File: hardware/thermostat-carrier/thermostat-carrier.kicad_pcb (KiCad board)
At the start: 2 copper layers, 100 x 100 mm, 82 parts, among them J1 24 VAC, J2 Calls 24 VAC, J3 USB-C 5 V in, J4 USB-A 5 V to display, J5 Display I2C, J6 Display IO6, J7 Room SHT45 (Qwiic), K1 AQV252G, K2 AQV252G, K3 AQV252G, K4 AQV252G, K5 AQV252G, K6 AQV252G, U1 LM2596HV, U10 H11AA1, U11 H11AA1, U12 H11AA1, U2 AMS1117-3.3, U3 MCP23017-E/SO, U4 TPS3823-33, U5 SC18IS602B, U6 Wio-SX1262, U7 H11AA1, U8 H11AA1, U9 H11AA1

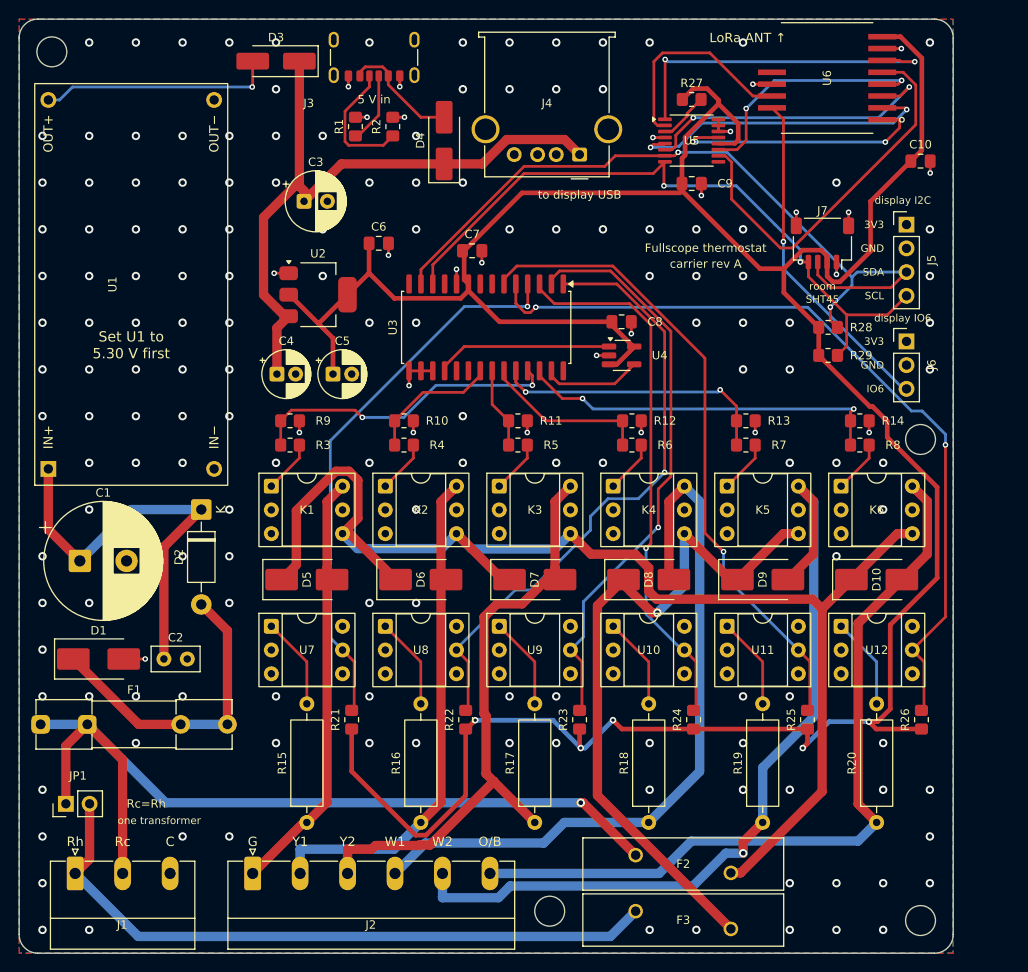
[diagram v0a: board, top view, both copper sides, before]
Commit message: Thermostat carrier: stack behind the Waveshare 4.3 on its own outline
The carrier now matches the display's 106 x 68 mm outline and screws to its
four M2.5 standoffs (measured from Waveshare's STEP model). SMD parts sit on
the wall side for JLC assembly; a right-edge notch clears the display's side
sockets, and short HY2.0 leads go to J5 (I2C) and J6 (IO6 for LoRa DIO1).

- Power: TPS54360B buck to 5.3 V replaces the LM2596 module; USB-C in for
  display-only use, USB-C out carries 5 V to the display.
- route.py: fan-out vias stay inside the outline and off exposed pads;
  pour islands are joined by vias, short bridges or a grid search
  (maze_bridge) for a GND track.
- gen_sch: PWR_FLAG on label nets (flag_nets) for the buck's VRAW input.
- make_fab: all-SMD JLC CPL/BOM for the thermostat carrier.
- DRC 0 violations, 0 unconnected, schematic parity clean; ERC clean.

Co-Authored-By: Claude Opus 5.5 <noreply@anthropic.com>
Claude-Session: https://claude.ai/code/session_011hFUPCDAe7urxnoDwvZQtt
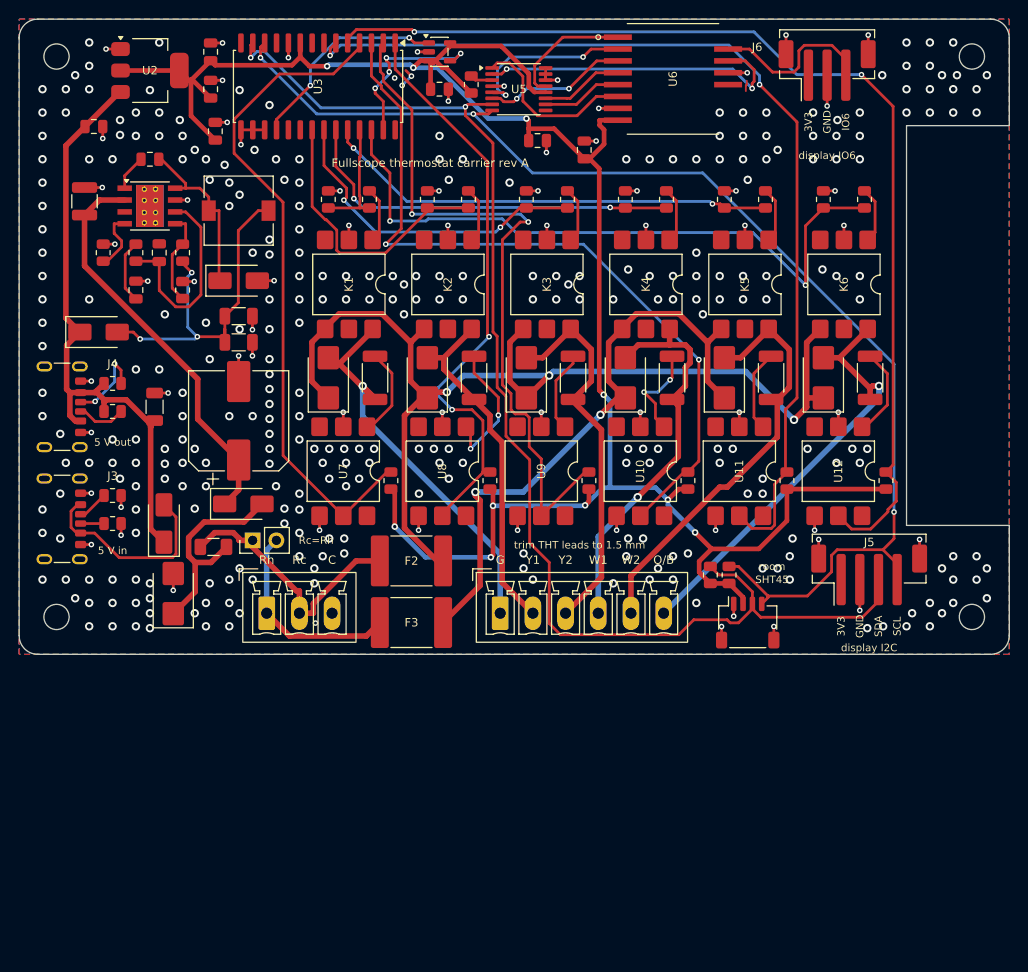
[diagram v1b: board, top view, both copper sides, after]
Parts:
- added C11: 0.1µF, Capacitor_SMD:C_0805_2012Metric, F.Cu at (64.0, 65.0)
- added C12: 22nF, Capacitor_SMD:C_0805_2012Metric, F.Cu at (62.5, 79.0)
- added C13: 100pF, Capacitor_SMD:C_0805_2012Metric, F.Cu at (65.0, 75.0)
- added C14: 22µF 16V, Capacitor_SMD:C_1206_3216Metric, F.Cu at (73.5, 81.8)
- added C15: 22µF 16V, Capacitor_SMD:C_1206_3216Metric, F.Cu at (73.5, 84.6)
- added D11: SS36, Diode_SMD:D_SMA, F.Cu at (73.5, 78.0)
- added L1: 22µH 2A, Inductor_SMD:L_7.3x7.3_H4.5, F.Cu at (73.5, 70.5)
- added R30: 243k, Resistor_SMD:R_0805_2012Metric, F.Cu at (59.0, 75.0)
- added R31: 56k, Resistor_SMD:R_0805_2012Metric, F.Cu at (67.5, 75.0)
- added R32: 10k, Resistor_SMD:R_0805_2012Metric, F.Cu at (67.5, 79.0)
- added R33: 6.8k, Resistor_SMD:R_0805_2012Metric, F.Cu at (62.5, 75.0)
- added R34: 56k, Resistor_SMD:R_0805_2012Metric, F.Cu at (60.0, 89.0)
- added R35: 56k, Resistor_SMD:R_0805_2012Metric, F.Cu at (60.0, 92.0)
- C1: value 1000µF 63V -> 220µF 63V; footprint Capacitor_THT:CP_Radial_D12.5mm_P5.00mm -> Capacitor_SMD:CP_Elec_10x10.5
- C10, C6, C7, C8, C9: footprint Capacitor_SMD:C_0805_2012Metric_Pad1.18x1.45mm_HandSolder -> Capacitor_SMD:C_0805_2012Metric
- C2: value 0.1µF -> 2.2µF 100V; footprint Capacitor_THT:C_Disc_D5.0mm_W2.5mm_P2.50mm -> Capacitor_SMD:C_1210_3225Metric
- C3: value 220µF 16V -> 22µF 16V; footprint Capacitor_THT:CP_Radial_D6.3mm_P2.50mm -> Capacitor_SMD:C_1206_3216Metric
- C4: value 10µF 16V -> 10µF 25V; footprint Capacitor_THT:CP_Radial_D5.0mm_P2.00mm -> Capacitor_SMD:C_0805_2012Metric
- C5: footprint Capacitor_THT:CP_Radial_D5.0mm_P2.00mm -> Capacitor_SMD:C_0805_2012Metric
- D1: value SMBJ48CA -> SMBJ40CA; footprint Diode_SMD:D_SMB_Handsoldering -> Diode_SMD:D_SMB
- D10, D5, D6, D7, D8, D9: footprint Diode_SMD:D_SMB_Handsoldering -> Diode_SMD:D_SMB
- D2: value 1N4007 -> S1M; footprint Diode_THT:D_DO-41_SOD81_P10.16mm_Horizontal -> Diode_SMD:D_SMA
- D3, D4: footprint Diode_SMD:D_SMA_Handsoldering -> Diode_SMD:D_SMA
- F1: value 0.5 A fast -> 0.5 A fast 63 V; footprint Fuse:Fuseholder_Clip-5x20mm_Littelfuse_111_Inline_P20.00x5.00mm_D1.05mm_Horizontal -> Fuse:Fuse_1206_3216Metric
- F2, F3: value 0ZRE0125FF -> 2920L110/60; footprint Fuse:Fuse_BelFuse_0ZRE0125FF_L21.2mm_W5.3mm -> Fuse:Fuse_2920_7451Metric
- H1, H2, H3, H4: value M3 -> M2.5; footprint MountingHole:MountingHole_3.2mm_M3_DIN965 -> MountingHole:MountingHole_2.7mm_M2.5_DIN965
- J1: footprint Connector_Phoenix_MC_HighVoltage:PhoenixContact_MC_1,5_3-G-5.08_1x03_P5.08mm_Horizontal -> Connector_Phoenix_MC:PhoenixContact_MCV_1,5_3-G-3.5_1x03_P3.50mm_Vertical
- J2: footprint Connector_Phoenix_MC_HighVoltage:PhoenixContact_MC_1,5_6-G-5.08_1x06_P5.08mm_Horizontal -> Connector_Phoenix_MC:PhoenixContact_MCV_1,5_6-G-3.5_1x06_P3.50mm_Vertical
- J4: value USB-A 5 V to display -> USB-C 5 V to display; footprint Connector_USB:USB_A_Molex_67643_Horizontal -> Connector_USB:USB_C_Receptacle_GCT_USB4125-xx-x_6P_TopMnt_Horizontal
- J5: footprint Connector_PinHeader_2.54mm:PinHeader_1x04_P2.54mm_Vertical -> Connector_JST:JST_PH_B4B-PH-SM4-TB_1x04-1MP_P2.00mm_Vertical
- J6: footprint Connector_PinHeader_2.54mm:PinHeader_1x03_P2.54mm_Vertical -> Connector_JST:JST_PH_B3B-PH-SM4-TB_1x03-1MP_P2.00mm_Vertical
- K1, K2, K3, K4, K5, K6: value AQV252G -> AQV252GS; footprint Package_DIP:DIP-6_W7.62mm_Socket -> Package_DIP:SMDIP-6_W9.53mm
- R1, R10, R11, R12, R13, R14, R2, R21, R22, R23, R24, R25, R26, R27, R28, R29, R3, R4, R5, R6, R7, R8, R9: footprint Resistor_SMD:R_0805_2012Metric_Pad1.20x1.40mm_HandSolder -> Resistor_SMD:R_0805_2012Metric
- R15, R16, R17, R18, R19, R20: value 4.7k ½W -> 4.7k 2010; footprint Resistor_THT:R_Axial_DIN0309_L9.0mm_D3.2mm_P12.70mm_Horizontal -> Resistor_SMD:R_2010_5025Metric
- U1: value LM2596HV -> TPS54360BDDAR; footprint hvac_carrier:LM2596HVS_Module -> Package_SO:TI_SO-PowerPAD-8_ThermalVias
- U10, U11, U12, U7, U8, U9: value H11AA1 -> H11AA1SM; footprint Package_DIP:DIP-6_W7.62mm_Socket -> Package_DIP:SMDIP-6_W9.53mm
- U4: footprint Package_TO_SOT_SMD:SOT-23-5_HandSoldering -> Package_TO_SOT_SMD:SOT-23-5
- moved H3 94.4 mm to (54.0, 114.0)
- moved H2 92.7 mm to (152.0, 54.0)
- moved J4 62.6 mm to (53.5, 91.5), turned to -90 degrees
- moved J3 61.2 mm to (53.5, 103.5), turned to -90 degrees
- moved H4 55.1 mm to (152.0, 114.0)
- moved R2 52.0 mm to (60.0, 104.0), turned to 0 degrees
- moved D4 50.8 mm to (65.5, 104.0)
- moved C2 49.7 mm to (57.0, 69.5), turned to 90 degrees
- moved R15 48.2 mm to (88.1, 88.4)
- moved R16 47.9 mm to (98.7, 88.4)
- moved R17 47.8 mm to (109.3, 88.4)
- moved R18 47.7 mm to (119.9, 88.4)
- moved R19 47.6 mm to (130.5, 88.4)
- moved R20 47.6 mm to (141.1, 88.4)
- moved R1 47.3 mm to (60.0, 101.0), turned to 0 degrees
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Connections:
- U1 pad 1: /VRAW -> /BOOT
- U1 pad 2: GND -> /VRAW
- U1 pad 3: /V5_BUCK -> unconnected-(U1-EN-Pad3)
- U1 pad 4: GND -> /RT
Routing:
- net +3V3: track 313.7 -> 228.0 mm, vias 5 -> 10
- net /RC_24V: track 96.5 -> 28.6 mm, vias 1 -> 0
- net GND: track 42.4 -> 108.6 mm, vias 179 -> 369
- net /SCL: track 73.1 -> 131.5 mm, vias 2 -> 3
- net /SDA: track 83.3 -> 138.0 mm
- net /RH_24V: track 72.0 -> 22.0 mm
- net /W2_24V: track 91.7 -> 45.5 mm, vias 1 -> 0
- net /OB_24V: track 84.2 -> 46.8 mm, vias 0 -> 1
- net /W1_24V: track 79.3 -> 42.3 mm, vias 0 -> 1
- net /SENSE_W2: track 69.2 -> 104.8 mm, vias 1 -> 2
- net /LORA_NRST: track 41.4 -> 8.61 mm
- net /DRV_OB: track 39.7 -> 71.6 mm
- net /SENSE_OB: track 86.0 -> 113.9 mm
- net /RCL_24V: track 143.4 -> 116.7 mm, vias 0 -> 3
- net /DRV_Y2: track 8.68 -> 35.1 mm, vias 0 -> 2
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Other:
- board size 100 x 100 mm -> 106 x 68 mm
- board text added: "5 V out"
- board text added: "Fullscope thermostat carrier rev A"
- board text added: "trim THT leads to 1.5 mm"
- board text removed: "5.30 V first"
- board text removed: "Fullscope thermostat"
- board text removed: "LoRa ANT ↑"
- board text removed: "Set U1 to"
- board text removed: "carrier rev A"
- board text removed: "one transformer"
- board text removed: "to display USB"
